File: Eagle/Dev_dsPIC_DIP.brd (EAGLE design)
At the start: 72.1 x 85.1 mm, 34 parts, among them IC1 DSPIC33FJ64MC802-SP, P1 Vin, P2 5V

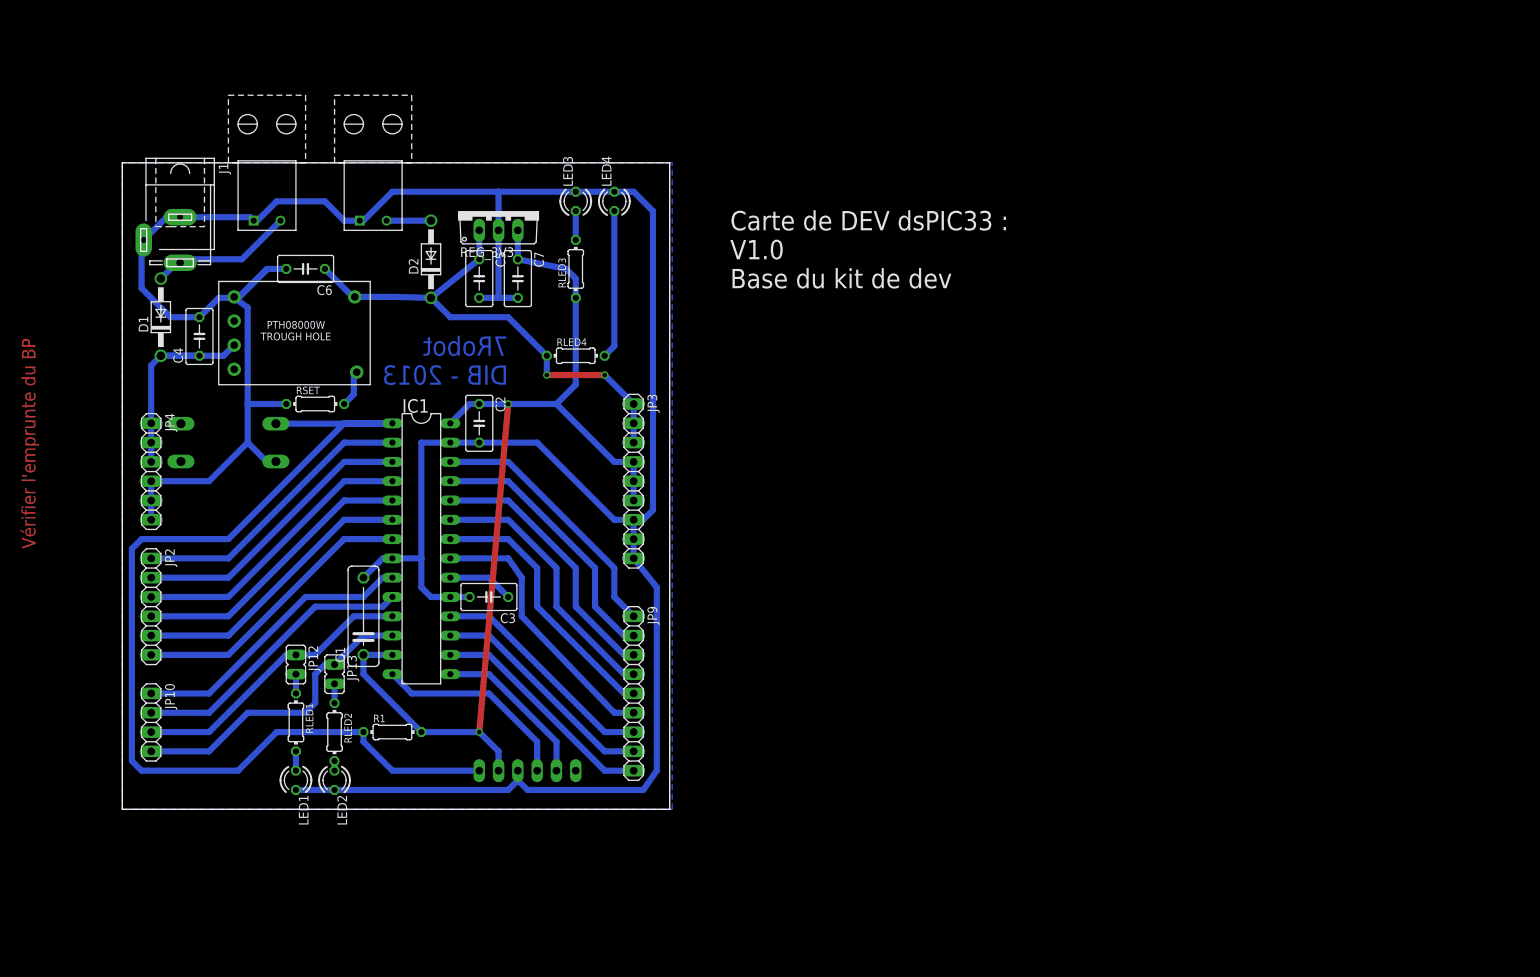
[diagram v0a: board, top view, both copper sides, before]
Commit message: Base dsPIC v1.1 & Shield Moteur sans connecteur
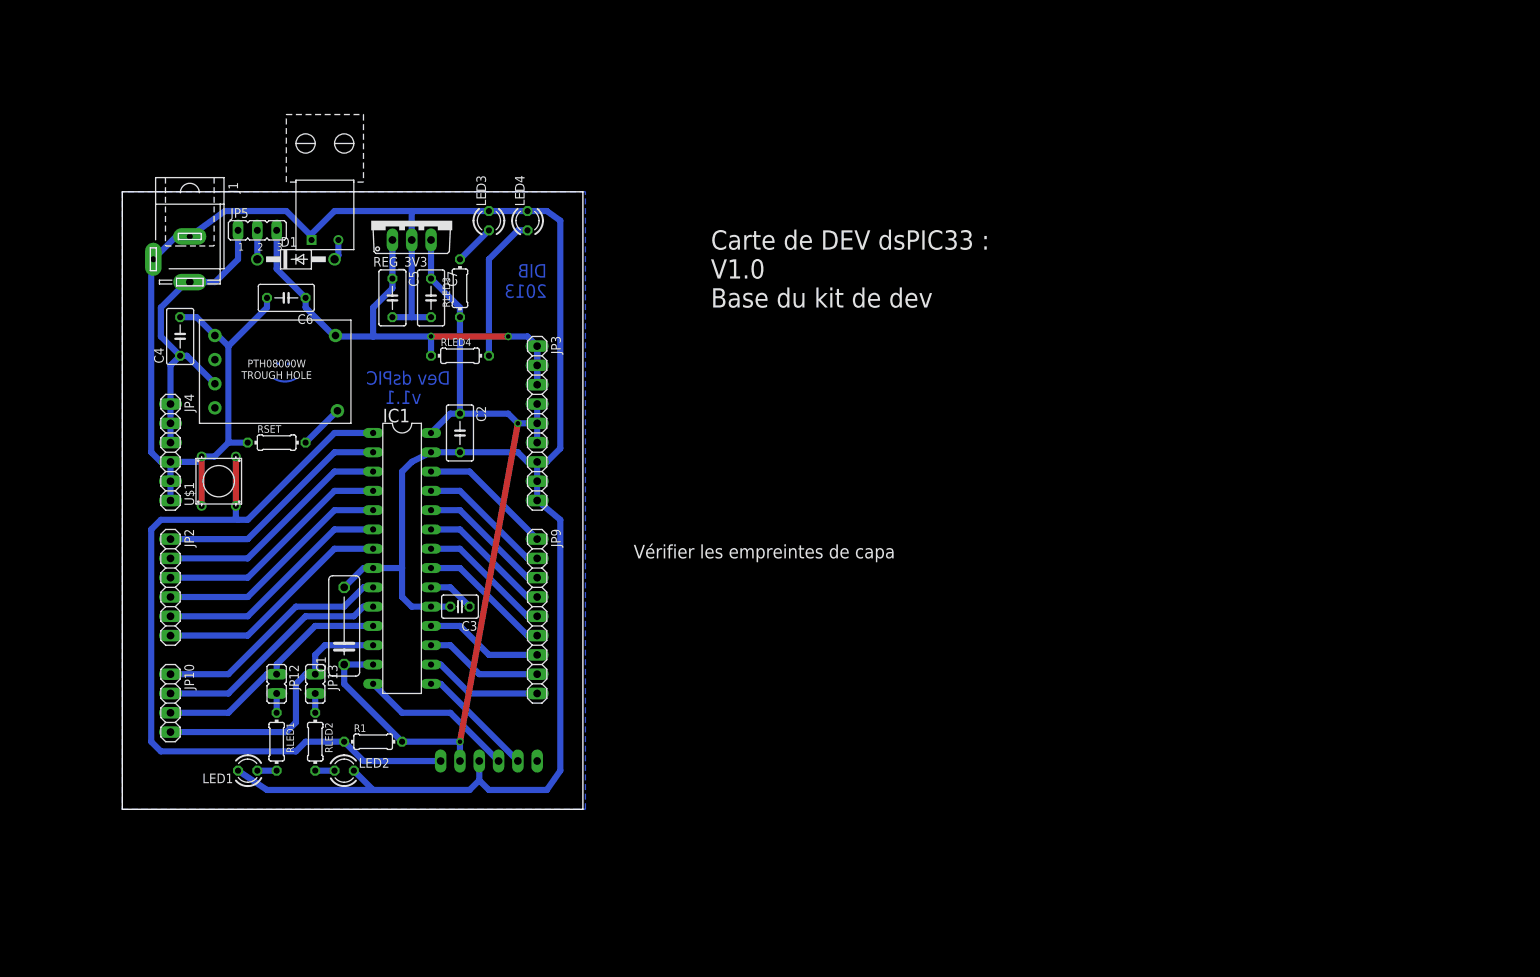
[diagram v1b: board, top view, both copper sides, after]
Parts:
- removed D2: 1N4004, diode:DO41-10
- removed P2: 5V, Perso:BORNIER_COUDEE_3.5
- removed S1: RACON12, switch-misc:RACON12
- added JP5: (no value), jumper:JP2
- added U$1: BP, Perso:BP
- C3: device rcl:C050-035X075 -> rcl:C025-030X050
- moved D1 19.3 mm to (22.9, 72.4), turned to 0 degrees
- moved JP9 16.3 mm to (54.6, 25.4)
- moved RLED3 15.5 mm to (44.5, 68.6)
- moved RLED4 15.2 mm to (44.5, 59.7)
- moved JP3 14.8 mm to (54.6, 50.8)
- moved LED3 11.7 mm to (48.3, 77.5)
- moved C5 11.7 mm to (35.6, 67.3)
- moved C7 11.7 mm to (40.6, 67.3)
- moved LED4 11.7 mm to (53.3, 77.5)
- moved REG_3V3 11.5 mm to (38.1, 77.5)
- moved P1 8.03 mm to (22.9, 73.7)
- moved RSET 7.18 mm to (20.3, 48.3)
- moved LED1 6.48 mm to (16.5, 5.08), turned to 180 degrees
- moved REG1 5.68 mm to (10.2, 50.8)
- moved JP1 5.24 mm to (48.3, 2.54)
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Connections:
- removed net VIN_P: C4.1, D1.C, JP4.1, JP4.2, JP4.3, REG1.3
- new net VCC: D1.C, JP5.2
- net 5V: now also JP5.3; no longer D2.C
- net MCLR: now also U$1.3, U$1.4; no longer S1.1
- net N$17: now also D1.A, P1.VCC; no longer D2.A, P2.VCC
- net PE: now also U$1.1, U$1.2; no longer P2.GND, S1.3
- net VIN: now also C4.1, JP4.1, JP4.2, JP4.3, JP5.1, REG1.3; no longer D1.A, P1.VCC
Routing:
- net PE: track 372.1 -> 338.1 mm
- net VIN_P: track 29.8 -> 0.00 mm
- net MCLR: track 135.6 -> 111.1 mm
- net VIN: track 19.4 -> 42.1 mm
- net +3V3: track 137.3 -> 114.9 mm
- net N$6: track 35.9 -> 17.7 mm
- net N$2: track 35.5 -> 17.7 mm
- net N$3: track 35.5 -> 17.7 mm
- net N$4: track 35.5 -> 17.7 mm
- net N$5: track 35.5 -> 17.7 mm
- net N$1: track 34.8 -> 17.7 mm
- net N$9: track 30.4 -> 15.5 mm
- net N$8: track 30.4 -> 15.5 mm
- net N$7: track 30.4 -> 15.5 mm
- net AN3: track 38.1 -> 31.4 mm
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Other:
- board size 72.1 x 85.1 mm -> 60.6 x 81.3 mm
- board text added: "( :"
- board text added: "DIB 2013"
- board text added: "Dev dsPIC"
- board text added: "Vérifier les empreintes de capa"
- board text added: "v1.1"
- board text removed: "7Robot DIB - 2013"
- board text removed: "Vérifier l'emprunte du BP"

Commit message: Ajout des trous pour fixation de la carte
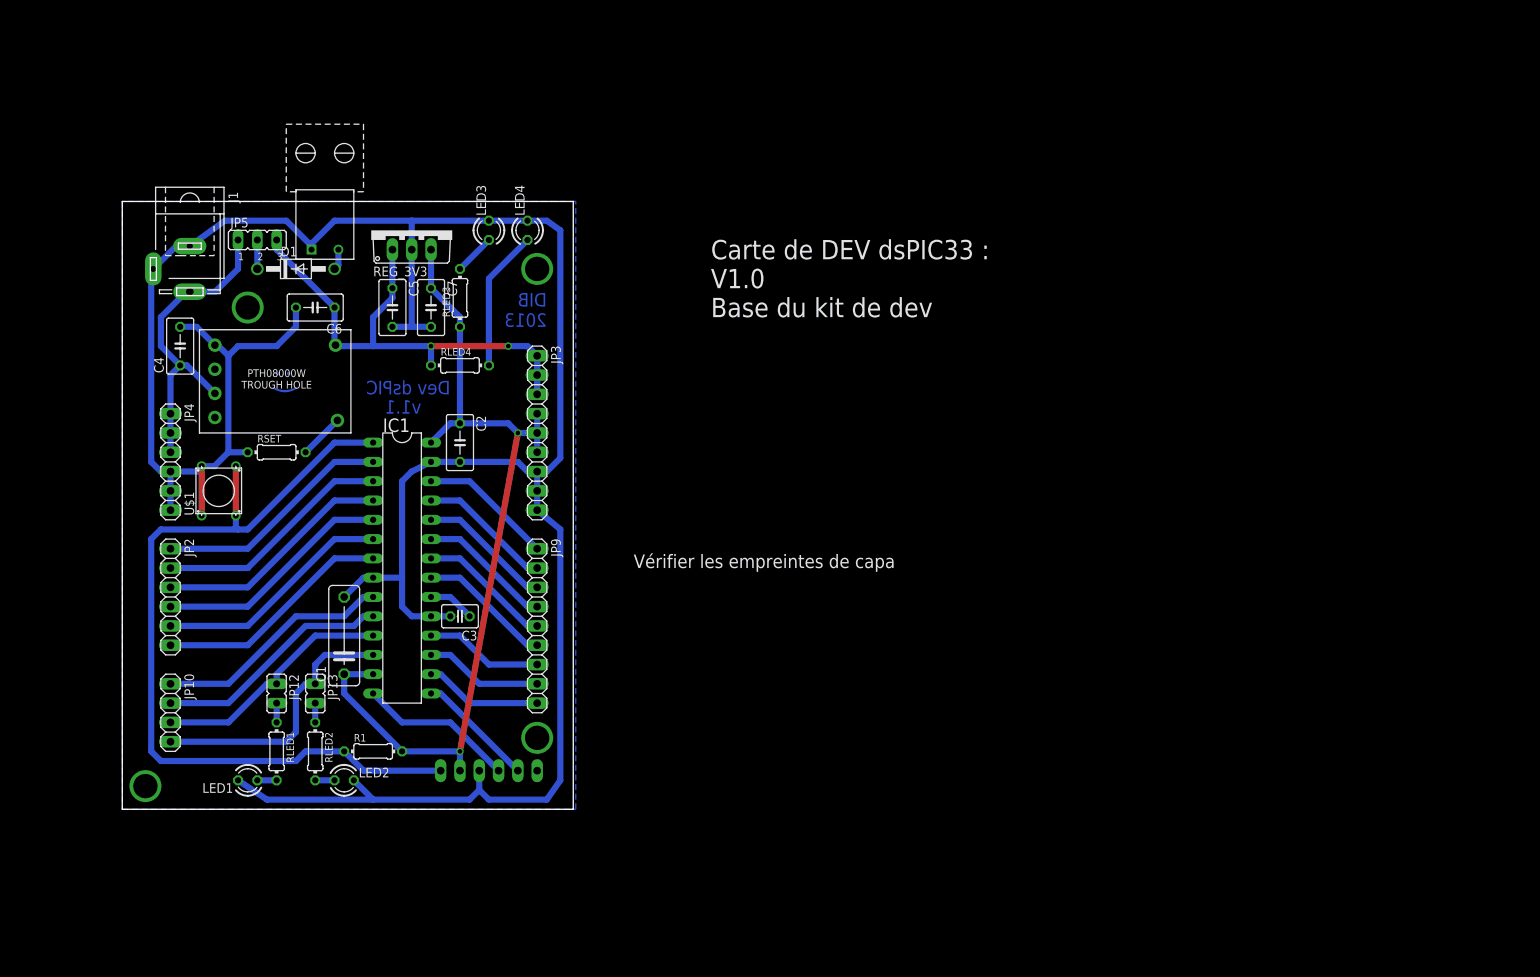
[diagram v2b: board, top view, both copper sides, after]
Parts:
- moved C6 4.02 mm to (25.4, 66.0)
- moved C2 1.27 mm to (44.5, 48.3)
- moved C3 1.27 mm to (44.5, 25.4)
- moved IC1 1.27 mm to (36.8, 31.8)
- moved JP4 1.27 mm to (6.35, 45.7)
- moved U$1 1.27 mm to (12.7, 41.9)
- moved JP10 1.27 mm to (6.35, 12.7)
- moved JP12 1.27 mm to (20.3, 15.2)
- moved JP13 1.27 mm to (25.4, 15.2)
- moved R1 1.27 mm to (33.0, 7.62)
- moved RLED1 1.27 mm to (20.3, 7.62)
- moved RLED2 1.27 mm to (25.4, 7.62)
- moved JP1 1.27 mm to (48.3, 1.27)
- moved LED1 1.27 mm to (16.5, 3.81)
- moved LED2 1.27 mm to (29.2, 3.81)
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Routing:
- net PE: track 338.1 -> 342.6 mm
- net N$21: track 19.4 -> 18.6 mm
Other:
- board size 60.6 x 81.3 mm -> 59.4 x 80 mm

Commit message: Petit changement au routage et au template
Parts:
- C1: device rcl:C102-043X133 -> rcl:C150-054X183
- C3: device rcl:C025-030X050 -> rcl:C050-035X075
- IC1: value DSPIC33FJ64MC802-SP -> DSPIC33FJ128MC802-SP
- R1, RLED1, RLED2, RLED3, RLED4, RSET: device rcl:0204/7 -> rcl:0207/10
- moved JP12 5.68 mm to (15.2, 12.7)
- moved JP13 2.84 mm to (24.1, 17.8)
- moved JP10 2.54 mm to (6.35, 15.2)
- moved JP2 2.54 mm to (6.35, 30.5)
- moved JP4 2.54 mm to (6.35, 48.3)
- moved U$1 1.80 mm to (14.0, 43.2), turned to 0 degrees
- moved RLED1 1.80 mm to (19.1, 8.89)
- moved RLED2 1.80 mm to (24.1, 8.89)
- moved RSET 1.80 mm to (19.1, 48.3)
- moved RLED4 1.27 mm to (43.2, 58.4)
- moved LED1 1.27 mm to (15.2, 3.81)
- moved LED2 1.27 mm to (27.9, 3.81)
- turned C3 to 270 degrees
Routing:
- net PE: track 342.6 -> 339.4 mm
- net N$15: track 2.54 -> 5.61 mm
- net VIN: track 42.1 -> 39.5 mm
- net VCAP: track 6.13 -> 3.81 mm
- net RB4: track 32.1 -> 30.4 mm
- net MCLR: track 111.1 -> 112.5 mm
- net +3V3: track 114.9 -> 113.6 mm
- net AN5: track 31.4 -> 30.4 mm
- net N$10: track 31.4 -> 30.4 mm
- net N$11: track 31.4 -> 30.4 mm
- net AN4: track 31.4 -> 30.4 mm
- net AN3: track 31.4 -> 30.4 mm
- net AN2: track 31.4 -> 30.4 mm
- net AN1: track 31.4 -> 30.4 mm
- net AN0: track 31.4 -> 30.4 mm
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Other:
- board text added: "Vérifier les empreintes de capa Refaire les empreintes de res avec une plus grosse pastille"
- board text removed: "Vérifier les empreintes de capa"

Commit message: Carte de DEV base presque finit
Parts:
- C3: device rcl:C050-035X075 -> rcl:E2,5-4R
- C4, C6: device rcl:C050-035X075 -> rcl:E3,5-8
- R1, RLED1, RLED2, RLED3, RLED4, RSET: device rcl:0207/10 -> Perso:RES_DIP_PERSO
- moved C6 14.4 mm to (35.6, 55.9), turned to 270 degrees
- moved C3 1.80 mm to (45.7, 24.1)
- moved D1 1.27 mm to (22.9, 69.8)
- moved RLED4 1.27 mm to (44.5, 58.4)
- moved REG1 1.27 mm to (11.4, 49.5)
- moved C4 0.25 mm to (7.37, 61.0), turned to 0 degrees
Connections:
- net 5V: now also C6.+; no longer C6.1
- net PE: now also C3.-, C4.-, C6.-; no longer C3.2, C4.2, C6.2
- net VCAP: now also C3.+; no longer C3.1
- net VIN: now also C4.+; no longer C4.1
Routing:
- net PE: track 339.4 -> 347.3 mm
- net 5V: track 70.6 -> 74.0 mm
- net VCAP: track 3.81 -> 6.13 mm
- net N$20: track 5.14 -> 6.69 mm
- net VCC: track 3.81 -> 5.08 mm
- net N$17: track 2.75 -> 4.02 mm
- net VIN: track 39.5 -> 40.4 mm
- net N$21: track 18.6 -> 17.8 mm
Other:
- board text added: "(1)"
- board text added: "(1) Connection des LEDs de debug"
- board text added: "3V3"
- board text added: "5V"
- board text added: "Carte de DEV dsPIC33 : V1.1 Base du kit de dev"
- board text added: "GND"
- board text added: "MCLR"
- board text added: "NC"
- board text added: "Refaire les empreintes de led avec une plus grosse pastille et passer aux 5mm"
- board text added: "Sélection de la tension du bornier : Gauche -> V > 6.1V Droit -> V = 5V"
- board text added: "VIN"
- board text removed: "Carte de DEV dsPIC33 : V1.0 Base du kit de dev"
- board text removed: "Dev dsPIC"
- board text removed: "Vérifier les empreintes de capa Refaire les empreintes de res avec une plus grosse pastille"
- board text removed: "v1.1"
